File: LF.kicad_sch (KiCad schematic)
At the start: 41 parts, among them J1 Conn_01x01_Pin, J2 Conn_01x01_Pin, J3 Conn_01x01_Pin, Q1 NMOS, Q2 NMOS, Q3 NMOS, Q4 NMOS, Q5 NMOS, Q6 NMOS, U1 MCT8329A1IREER, U2 OPA2196xDGK

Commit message: The great decluttering
Moved all possible controls to I2C, part selection commenced, IOs assigned pending comms schema
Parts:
- removed C10: 100n, Capacitor_SMD:C_0603_1608Metric, symbol Device:C
- removed R10: 50m0R, Resistor_SMD:R_1206_3216Metric, symbol Device:R
- removed R11, R12, R13, R139, R14: R, Resistor_SMD:R_0603_1608Metric_Pad0.98x0.95mm_HandSolder, symbol Device:R
- removed U2: OPA2196xDGK, Package_SO:VSSOP-8_3x3mm_P0.65mm, symbol Amplifier_Operational:OPA2196xDGK
- Q1, Q2, Q3, Q4, Q5, Q6: value NMOS -> GSFP6016; footprint (none) -> Package_DFN_QFN:PQFN-8-EP_6x5mm_P1.27mm_Generic
- R1: renamed from R16; value R -> 20K
- R11: renamed from R7; value 50m0R -> 10m0R
- R2: renamed from R15; value R -> 180K
- renumbered C11 to C1, C9 to C10, C6 to C2, C5 to C3, C1 to C4, C7 to C5, C4 to C6, C2 to C7, C3 to C8, C8 to C9, R18 to R10, R8 to R12, R9 to R13, R1 to R3, R2 to R4, R3 to R5, R4 to R6, R5 to R7, R6 to R8, R17 to R9
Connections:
- net LF_{VDD}: now also C1.1, C2.1, C5.1, U1.5 (PVDD)
- net LF_{VS}: now also R1.1, R2.2
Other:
- note added: "==TODO== NONE Must shake HV design tendancies - unified power domain ==NOTAMS== TOLERANCES All values specified are 1% unless otherwise defined I2C I2C comms only DRIVER All critical driver operations except sleep are available over I2C BOOTST Bootstrap capacitors sized for 100% duty cycle operation R_{G} R_{G} sized for UP TO 1uC gate at f = 25KHz"
- note removed: "==TODO== Literally everything DIVIDERS AND GAIN Gain and dividers will be calculated before load ==NOTAMS== TOLERANCES All values specified are 1% unless otherwise defined I2C I2C comms only ISNS High side sense for whole current metering ONLY BOOTST Bootstrap capacitors sized for 100% duty cycle operation R_{G} R_{G} sized for UP TO 1uC gate at f = 25KHz FEEDBACK Feedback values TBD"
- moved on the sheet: C1, C10, C2, C3, C4, C5, C6, C7, C8, C9, J1, J2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

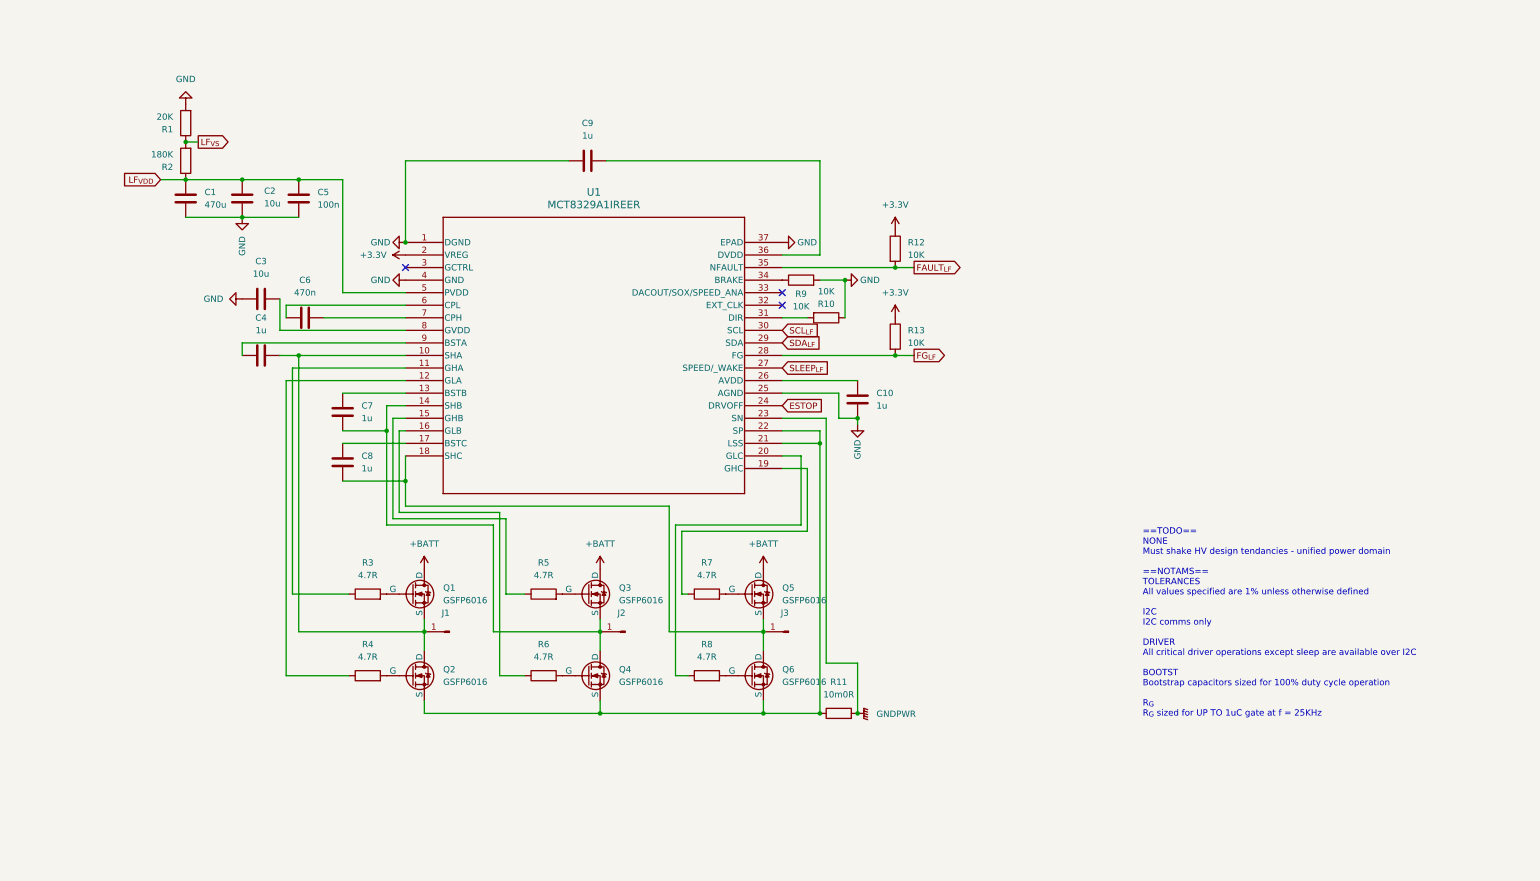
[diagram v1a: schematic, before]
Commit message: Powerstage
Powerstage layout, non critical changes to schematic
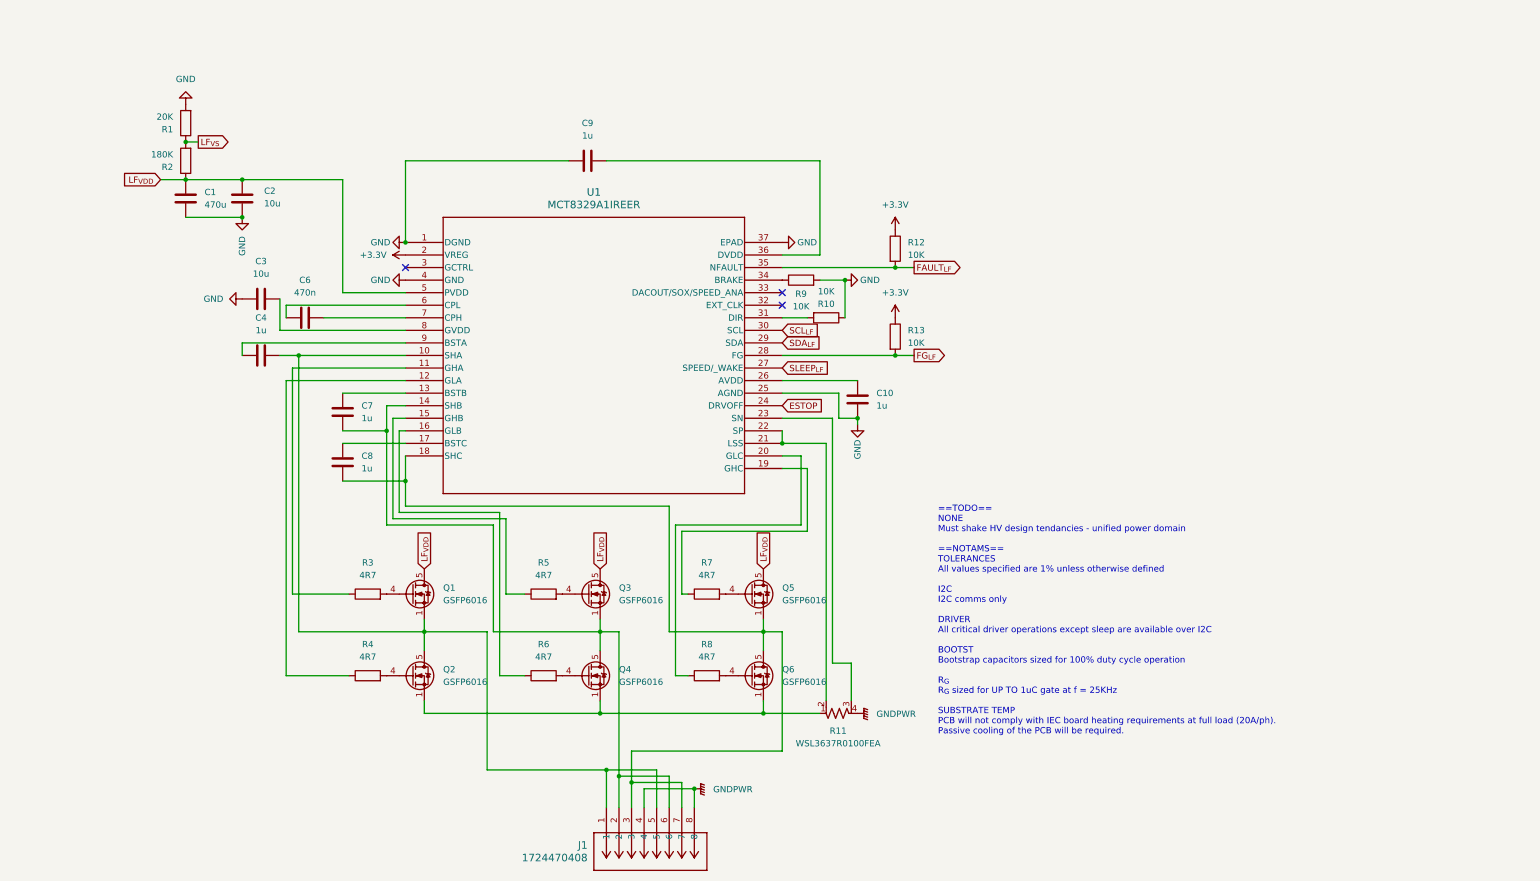
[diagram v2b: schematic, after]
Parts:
- removed C5: 100n, Capacitor_SMD:C_0603_1608Metric, symbol Device:C
- removed J1, J2, J3: Conn_01x01_Pin, symbol Connector:Conn_01x01_Pin
- removed Q1, Q2, Q3, Q4, Q5, Q6: GSFP6016, Package_DFN_QFN:PQFN-8-EP_6x5mm_P1.27mm_Generic, symbol Simulation_SPICE:NMOS
- removed R11: 10m0R, Resistor_SMD:R_1206_3216Metric, symbol Device:R
- added J1: 1724470408, footprints:CONN08_1724470408_MOL, symbol 1724470408:1724470408
- added Q1, Q2, Q3, Q4, Q5, Q6: GSFP6016, Package_SO:PowerPAK_SO-8_Single, symbol Transistor_FET:SiR696DP
- added R11: WSL3637R0100FEA, WSL3637_VIS, symbol WSL3637R0100FEA:WSL3637R0100FEA
- C1: footprint Capacitor_SMD:C_0603_1608Metric -> Capacitor_THT:CP_Radial_D10.0mm_P5.00mm
- C10, C4, C6, C7, C8, C9: footprint Capacitor_SMD:C_0603_1608Metric -> Capacitor_SMD:C_0201_0603Metric
- C2: footprint Capacitor_SMD:C_0603_1608Metric -> Capacitor_SMD:C_1210_3225Metric
- C3: footprint Capacitor_SMD:C_0603_1608Metric -> Capacitor_SMD:C_0402_1005Metric
- R1, R10, R12, R13, R2, R9: footprint Resistor_SMD:R_0603_1608Metric_Pad0.98x0.95mm_HandSolder -> Resistor_SMD:R_0201_0603Metric
- R3, R4, R5, R6, R7, R8: value 4.7R -> 4R7; footprint Resistor_SMD:R_1206_3216Metric -> Resistor_SMD:R_0603_1608Metric
- U1: footprint footprints:WQFN36_REE_TEX -> WQFN36_REE_TEX
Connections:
- net GNDPWR: now also J1.4, J1.8, R11.4; no longer U1.23 (SN)
- net LF_{VDD}: now also Q1.5 (D), Q3.5 (D), Q5.5 (D)
- net at C7.2, U1.14 (SHB): now also J1.2, J1.6, Q3.1 (S), Q3.2 (S), Q3.3 (S), Q4.5 (D)
- net at C6.1: now also U1.7 (CPH); no longer U1.6 (CPL)
- net at C6.2: now also U1.6 (CPL); no longer U1.7 (CPH)
- net at R7.2: now also Q5.4 (G)
- net at C8.2, U1.18 (SHC): now also J1.3, J1.7, Q5.1 (S), Q5.2 (S), Q5.3 (S), Q6.5 (D)
- net at R3.2: now also Q1.4 (G)
- net at C4.1, U1.10 (SHA): now also J1.1, J1.5, Q1.1 (S), Q1.2 (S), Q1.3 (S), Q2.5 (D)
- net at R8.2: now also Q6.4 (G)
- net at R6.2: now also Q4.4 (G)
- net at U1.21 (LSS), U1.22 (SP): now also R11.2
- net at R5.2: now also Q3.4 (G)
- net at R4.2: now also Q2.4 (G)
- new net: Q2.1 (S), Q2.2 (S), Q2.3 (S), Q4.1 (S), Q4.2 (S), Q4.3 (S), Q6.1 (S), Q6.2 (S), Q6.3 (S), R11.1
- new net: R11.3, U1.23 (SN)
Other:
- note added: "==TODO== NONE Must shake HV design tendancies - unified power domain ==NOTAMS== TOLERANCES All values specified are 1% unless otherwise defined I2C I2C comms only DRIVER All critical driver operations except sleep are available over I2C BOOTST Bootstrap capacitors sized for 100% duty cycle operation R_{G} R_{G} sized for UP TO 1uC gate at f = 25KHz SUBSTRATE TEMP PCB will not comply with IEC boar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"
- note removed: "==TODO== NONE Must shake HV design tendancies - unified power domain ==NOTAMS== TOLERANCES All values specified are 1% unless otherwise defined I2C I2C comms only DRIVER All critical driver operations except sleep are available over I2C BOOTST Bootstrap capacitors sized for 100% duty cycle operation R_{G} R_{G} sized for UP TO 1uC gate at f = 25KHz"
- moved on the sheet: C6
